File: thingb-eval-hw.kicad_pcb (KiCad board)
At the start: 2 copper layers, 100 x 100 mm, 70 parts, among them J1 USB_C_Receptacle_USB2.0, J2 Conn_01x06, J3 Conn_01x05, J4 SIM_Card, Q1 S9015, Q2 RU8205G, SW1 SW_Push, SW2 SW_Push, SW3 TSWB-3N-CB, U1 ESP32-WROVER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

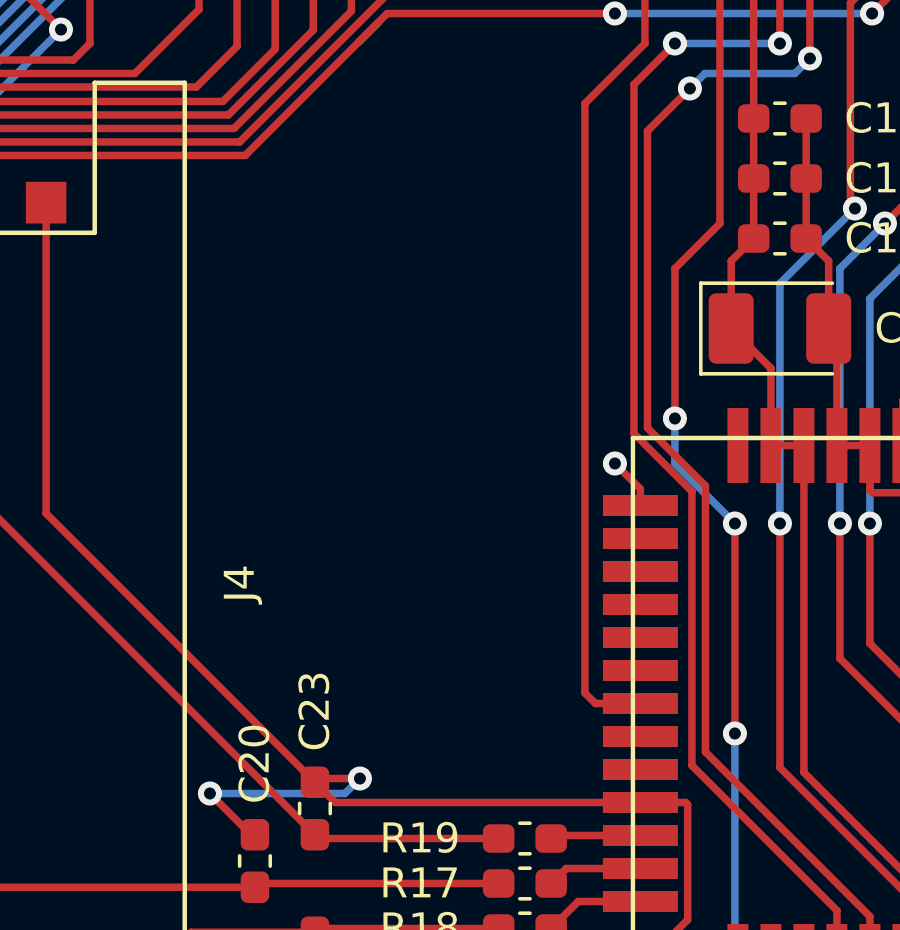
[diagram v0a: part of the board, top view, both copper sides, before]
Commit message: add name, date, and revision to silkscreen
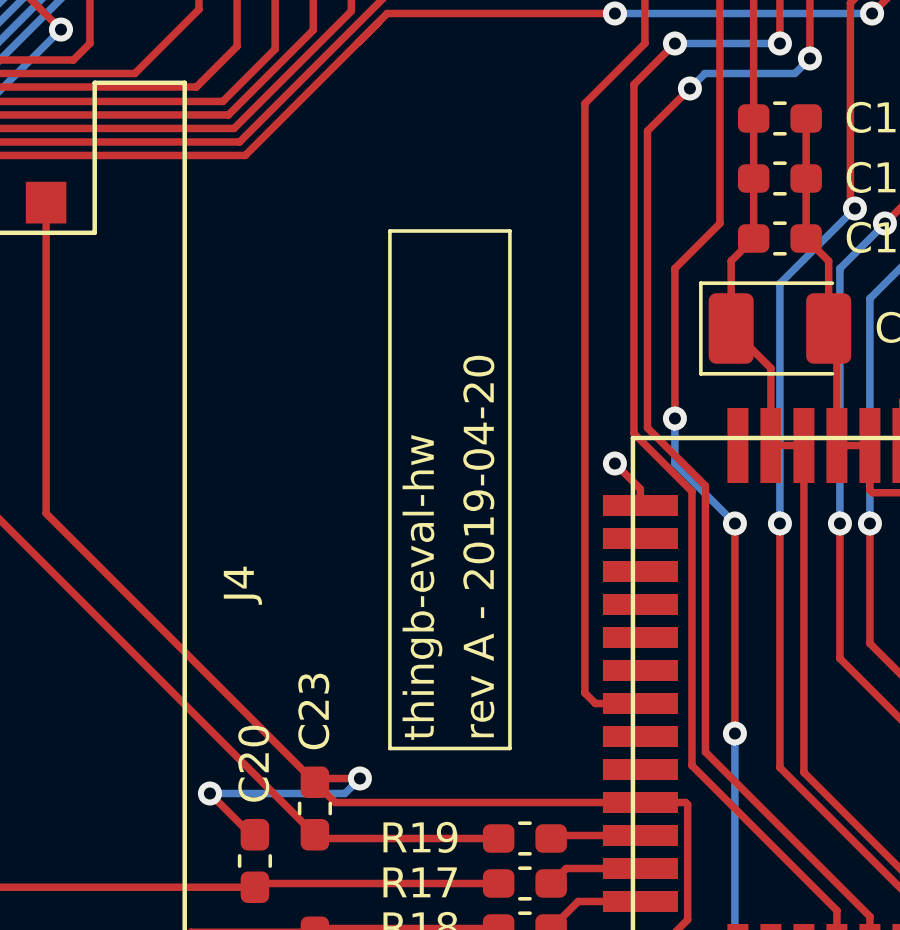
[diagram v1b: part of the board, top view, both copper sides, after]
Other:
- board text added: "rev A - 2019-04-20"
- board text added: "thingb-eval-hw"
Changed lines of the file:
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@@
   (general
     (thickness 1.6)
-    (drawings 17)
+    (drawings 23)
     (tracks 1101)
     (zones 0)
@@
     )
   )
+  (gr_line (start 121 86.25) (end 117 86.25) (layer F.SilkS) (width 0.12))
+  (gr_line (start 121 103.5) (end 121 86.25) (layer F.SilkS) (width 0.12))
+  (gr_line (start 117 103.5) (end 121 103.5) (layer F.SilkS) (width 0.12))
+  (gr_line (start 117 86.25) (end 117 103.5) (layer F.SilkS) (width 0.12))
+  (gr_text "rev A - 2019-04-20" (at 120 103.25 90) (layer F.SilkS)
+    (effects (font (size 1 1) (thickness 0.15)) (justify left))
+  )
+  (gr_text thingb-eval-hw (at 118 103.25 90) (layer F.SilkS)
+    (effects (font (size 1 1) (thickness 0.15)) (justify left))
+  )
   (gr_text DBG_TXD (at 144 86.12) (layer F.SilkS)
